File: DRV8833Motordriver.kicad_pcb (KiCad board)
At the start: 2 copper layers, 8 parts, among them J1 Conn_01x06_Pin, J2 Conn_01x06_Pin, U1 DRV8833PWP

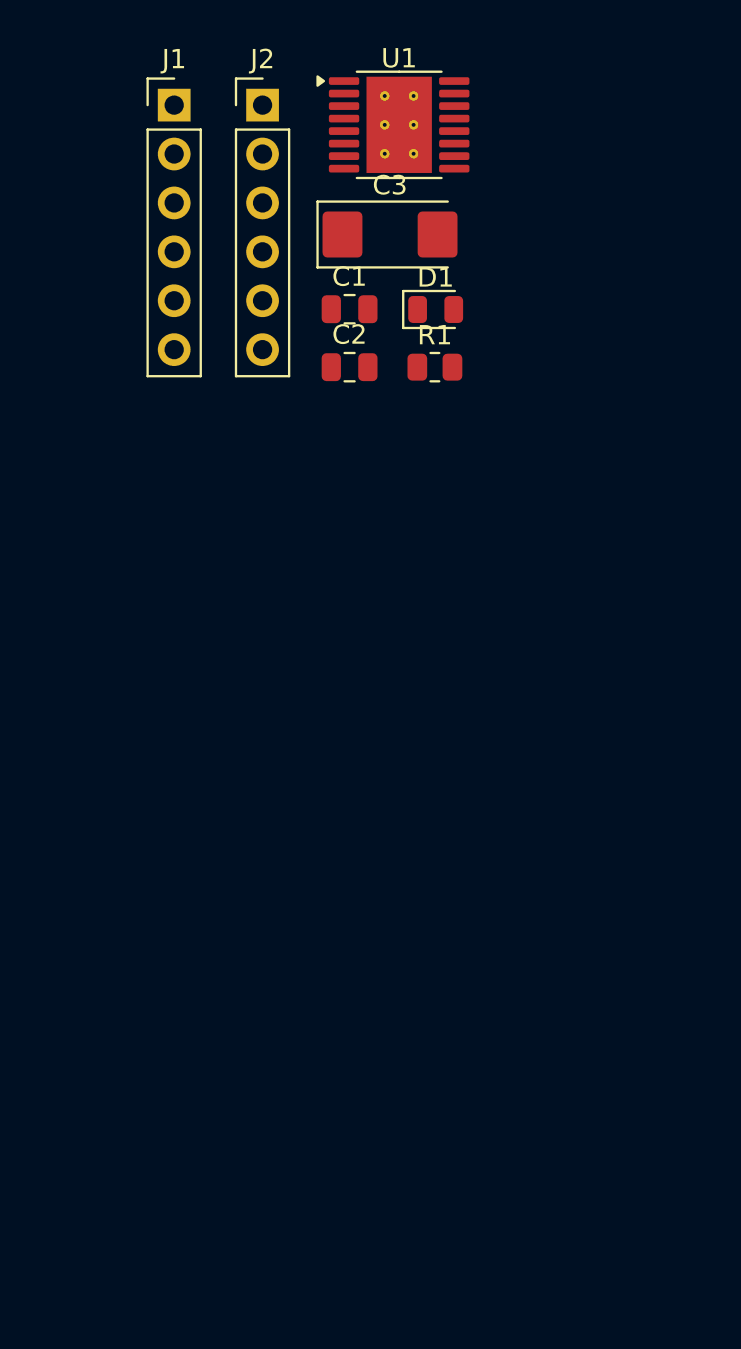
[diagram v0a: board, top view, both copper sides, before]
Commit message: Placed Components at correct Place
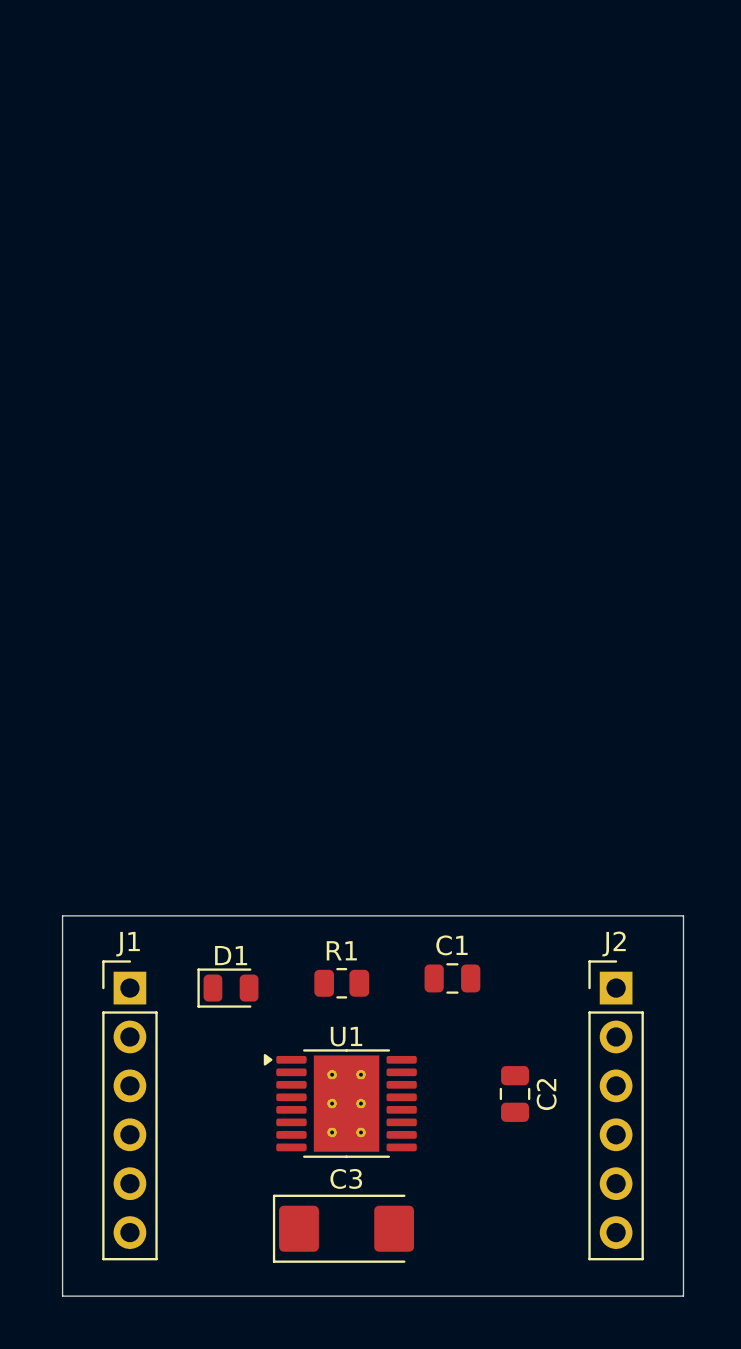
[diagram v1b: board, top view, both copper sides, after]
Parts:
- moved C3 51.7 mm to (148.5, 112.8)
- moved U1 50.9 mm to (148.5, 106.2)
- moved J2 49.4 mm to (162.5, 100.2)
- moved J1 45.9 mm to (137.2, 100.2)
- moved C2 38.7 mm to (157.2, 105.8), turned to -90 degrees
- moved D1 36.8 mm to (142.5, 100.2)
- moved C1 35.2 mm to (154.0, 99.8)
- moved R1 32.4 mm to (148.2, 100.0)
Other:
- board outline added: 32.2 x 19.8 mm
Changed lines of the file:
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@@
 	(footprint "Capacitor_Tantalum_SMD:CP_EIA-6032-20_AVX-F"
 		(layer "F.Cu")
-		(at 150.7575 61.11)
+		(at 148.5 112.75)
 		(descr "Tantalum Capacitor SMD AVX-F (6032-20 Metric), IPC-7352 nominal, (Body size from: http://www.kemet.com/Lists/ProductCatalog/Attachments/253/KEM_TC101_STD.pdf), generated with kicad-footprint-generator")
 		(tags "capacitor tantalum")
@@
 	(footprint "LED_SMD:LED_0805_2012Metric"
 		(layer "F.Cu")
-		(at 153.1275 65.005)
+		(at 142.5 100.25)
 		(descr "LED SMD 0805 (2012 Metric), square (rectangular) end terminal, IPC-7351 nominal, (Body size source: https://docs.google.com/spreadsheets/d/1BsfQQcO9C6DZCsRaXUlFlo91Tg2WpOkGARC1WS5S8t0/edit?usp=sharing), generated with kicad-footprint-generator")
 		(tags "LED")
@@
 	(footprint "Connector_PinHeader_2.54mm:PinHeader_1x06_P2.54mm_Vertical"
 		(layer "F.Cu")
-		(at 144.1375 54.39)
+		(at 162.5 100.25)
 		(descr "Through hole straight pin header, 1x06, 2.54mm pitch, single row")
 		(tags "Through hole pin header THT 1x06 2.54mm single row")
@@
 	(footprint "Package_SO:HTSSOP-16-1EP_4.4x5mm_P0.65mm_EP3.4x5mm_Mask2.46x2.31mm_ThermalVias"
 		(layer "F.Cu")
-		(at 151.2325 55.415)
+		(at 148.5 106.25)
 		(descr "HTSSOP, 16 Pin (http://www.analog.com/media/en/technical-documentation/data-sheets/LTC7810.pdf), generated with kicad-footprint-generator ipc_gullwing_generator.py")
 		(tags "HTSSOP SO")
@@
 	(footprint "Connector_PinHeader_2.54mm:PinHeader_1x06_P2.54mm_Vertical"
 		(layer "F.Cu")
-		(at 139.5475 54.39)
+		(at 137.25 100.25)
 		(descr "Through hole straight pin header, 1x06, 2.54mm pitch, single row")
 		(tags "Through hole pin header THT 1x06 2.54mm single row")
@@
 	(footprint "Resistor_SMD:R_0805_2012Metric"
 		(layer "F.Cu")
-		(at 153.0875 68)
+		(at 148.25 100)
 		(descr "Resistor SMD 0805 (2012 Metric), square (rectangular) end terminal, IPC-7351 nominal, (Body size source: IPC-SM-782 page 72, https://www.pcb-3d.com/wordpress/wp-content/uploads/ipc-sm-782a_amendment_1_and_2.pdf), generated with kicad-footprint-generator")
 		(tags "resistor")
@@
 	(footprint "Capacitor_SMD:C_0805_2012Metric"
 		(layer "F.Cu")
-		(at 148.6575 64.99)
+		(at 154 99.75)
 		(descr "Capacitor SMD 0805 (2012 Metric), square (rectangular) end terminal, IPC-7351 nominal, (Body size source: IPC-SM-782 page 76, https://www.pcb-3d.com/wordpress/wp-content/uploads/ipc-sm-782a_amendment_1_and_2.pdf, https://docs.google.com/spreadsheets/d/1BsfQQcO9C6DZCsRaXUlFlo91Tg2WpOkGARC1WS5S8t0/edit?usp=sharing), generated with kicad-footprint-generator")
 		(tags "capacitor")
@@
 	(footprint "Capacitor_SMD:C_0805_2012Metric"
 		(layer "F.Cu")
-		(at 148.6575 68)
+		(at 157.25 105.75 -90)
 		(descr "Capacitor SMD 0805 (2012 Metric), square (rectangular) end terminal, IPC-7351 nominal, (Body size source: IPC-SM-782 page 76, https://www.pcb-3d.com/wordpress/wp-content/uploads/ipc-sm-782a_amendment_1_and_2.pdf, https://docs.google.com/spreadsheets/d/1BsfQQcO9C6DZCsRaXUlFlo91Tg2WpOkGARC1WS5S8t0/edit?usp=sharing), generated with kicad-footprint-generator")
 		(tags "capacitor")
 		(property "Reference" "C2"
-			(at 0 -1.68 0)
+			(at 0 -1.68 90)
 			(layer "F.SilkS")
 			(effects
@@
 		)
 		(property "Value" "2.2uF"
-			(at 0 1.68 0)
+			(at 0 1.68 90)
 			(layer "F.Fab")
 			(effects
@@
 		)
 		(property "Datasheet" ""
-			(at 0 0 0)
+			(at 0 0 90)
 			(layer "F.Fab")
 			(hide yes)
@@
 		)
 		(property "Description" "Unpolarized capacitor"
-			(at 0 0 0)
+			(at 0 0 90)
 			(layer "F.Fab")
 			(hide yes)
@@
 		(attr smd)
 		(fp_line
+			(start -0.261252 0.735)
+			(end 0.261252 0.735)
+			(stroke
+				(width 0.12)
+				(type solid)
+			)
+			(layer "F.SilkS")
+		)
+		(fp_line
 			(start -0.261252 -0.735)
 			(end 0.261252 -0.735)
@@
 		)
 		(fp_line
-			(start -0.261252 0.735)
-			(end 0.261252 0.735)
-			(stroke
-				(width 0.12)
-				(type solid)
-			)
-			(layer "F.SilkS")
+			(start -1.7 0.98)
+			(end -1.7 -0.98)
+			(stroke
+				(width 0.05)
+				(type solid)
+			)
+			(layer "F.CrtYd")
+		)
+		(fp_line
+			(start 1.7 0.98)
+			(end -1.7 0.98)
+			(stroke
+				(width 0.05)
+				(type solid)
+			)
+			(layer "F.CrtYd")
 		)
 		(fp_line
@@
 		)
 		(fp_line
-			(start -1.7 0.98)
-			(end -1.7 -0.98)
-			(stroke
-				(width 0.05)
-				(type solid)
-			)
-			(layer "F.CrtYd")
-		)
-		(fp_line
 			(start 1.7 -0.98)
 			(end 1.7 0.98)
@@
 		)
 		(fp_line
-			(start 1.7 0.98)
-			(end -1.7 0.98)
-			(stroke
-				(width 0.05)
-				(type solid)
-			)
-			(layer "F.CrtYd")
+			(start -1 0.625)
+			(end -1 -0.625)
+			(stroke
+				(width 0.1)
+				(type solid)
+			)
+			(layer "F.Fab")
+		)
+		(fp_line
+			(start 1 0.625)
+			(end -1 0.625)
+			(stroke
+				(width 0.1)
+				(type solid)
+			)
+			(layer "F.Fab")
 		)
 		(fp_line
@@
 		)
 		(fp_line
-			(start -1 0.625)
-			(end -1 -0.625)
-			(stroke
-				(width 0.1)
-				(type solid)
-			)
-			(layer "F.Fab")
-		)
-		(fp_line
 			(start 1 -0.625)
 			(end 1 0.625)
@@
 			(layer "F.Fab")
 		)
-		(fp_line
-			(start 1 0.625)
-			(end -1 0.625)
-			(stroke
-				(width 0.1)
-				(type solid)
-			)
-			(layer "F.Fab")
-		)
 		(fp_text user "${REFERENCE}"
-			(at 0 0 0)
+			(at 0 0 90)
 			(layer "F.Fab")
 			(effects
@@
 		)
 		(pad "1" smd roundrect
-			(at -0.95 0)
+			(at -0.95 0 270)
 			(size 1 1.45)
 			(layers "F.Cu" "F.Mask" "F.Paste")
@@
 		)
 		(pad "2" smd roundrect
-			(at 0.95 0)
+			(at 0.95 0 270)
 			(size 1 1.45)
 			(layers "F.Cu" "F.Mask" "F.Paste")
@@
 		)
 	)
+	(gr_rect
+		(start 133.75 96.5)
+		(end 166 116.25)
+		(stroke
+			(width 0.05)
+			(type default)
+		)
+		(fill no)
+		(layer "Edge.Cuts")
+	)
 	(embedded_fonts no)

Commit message: Placed Tracks for the Footprints
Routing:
- net /VCC: track 0.00 -> 59.1 mm, vias 0 -> 1
- net GND: track 0.00 -> 51.6 mm, vias 0 -> 1
- net /BOUT1: track 0.00 -> 19.8 mm, vias 0 -> 1
- net /BIN2: track 0.00 -> 16.7 mm
- net /AIN1: track 0.00 -> 12.7 mm
- net /BIN1: track 0.00 -> 11.9 mm
- net /AIN2: track 0.00 -> 11.9 mm
- net /FAULT: track 0.00 -> 10.2 mm
- net /BOUT2: track 0.00 -> 9.98 mm
- net /SLEEP: track 0.00 -> 9.93 mm
- net /AOUT1: track 0.00 -> 9.15 mm
- net /AOUT2: track 0.00 -> 8.63 mm
- net Net-(D1-K): track 0.00 -> 6.53 mm
- net Net-(U1-VCP): track 0.00 -> 6.10 mm

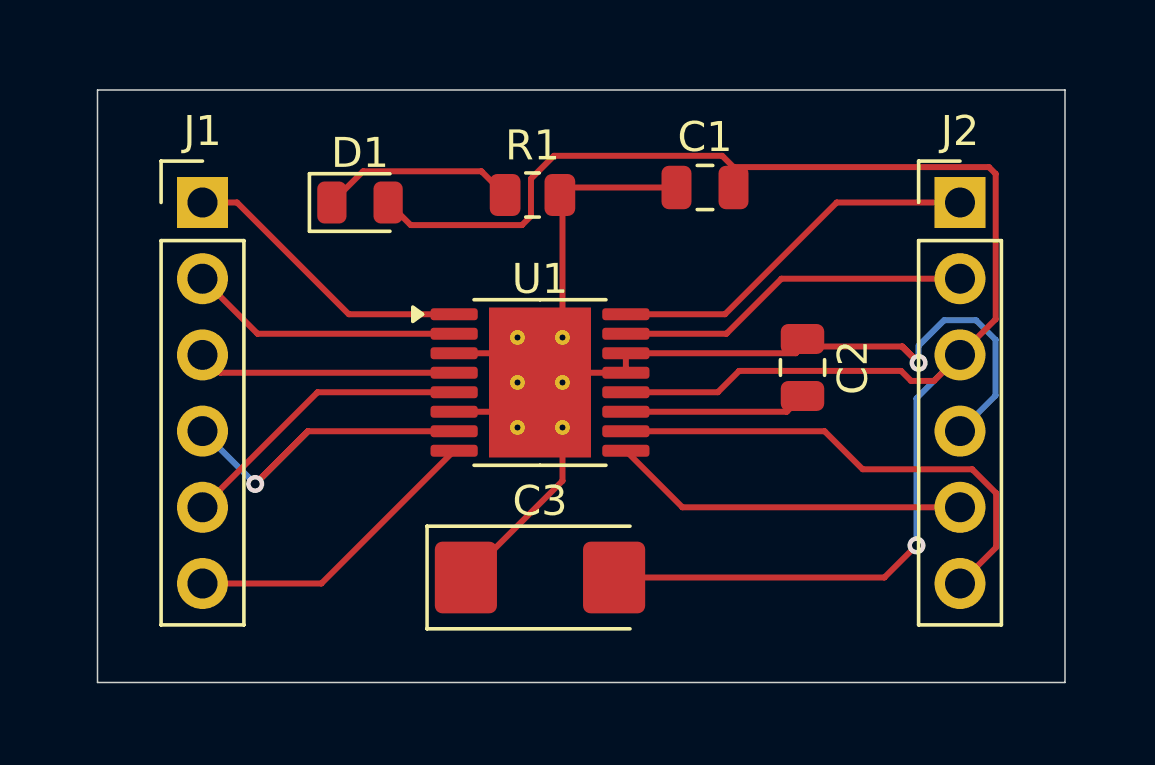
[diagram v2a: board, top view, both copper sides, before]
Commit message: Added Filled Zones
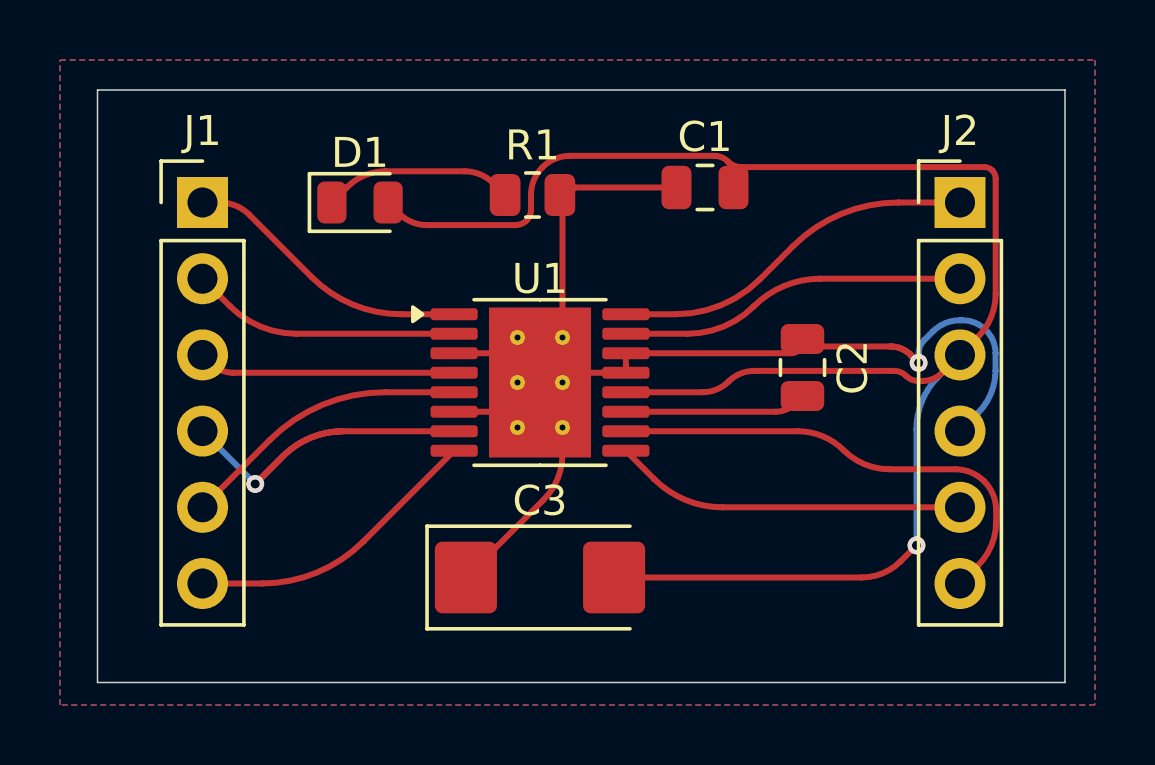
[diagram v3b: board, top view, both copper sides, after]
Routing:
- net /BOUT1: track 19.8 -> 17.2 mm
- net GND: track 51.6 -> 50.5 mm
- added copper zone on B.Cu, net GND
- added copper zone on F.Cu, net GND
